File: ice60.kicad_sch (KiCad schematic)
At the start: 31 parts, among them J1 SWD, J2 JST SH 4-pin, SW1 SW_Push, U1 RP2040, U2 W25Q128JVS, U3 XC6206PxxxMR-Regulator_Linear, U4 SRV05-4, Y1 12MHz

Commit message: rearrange schematic
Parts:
- renumbered C4 to C2, C5 to C3, C2 to C4, C3 to C5
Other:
- moved on the sheet: C1, C10, C11, C12, C13, C14, C15, C16, C17, C2, C3, C4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

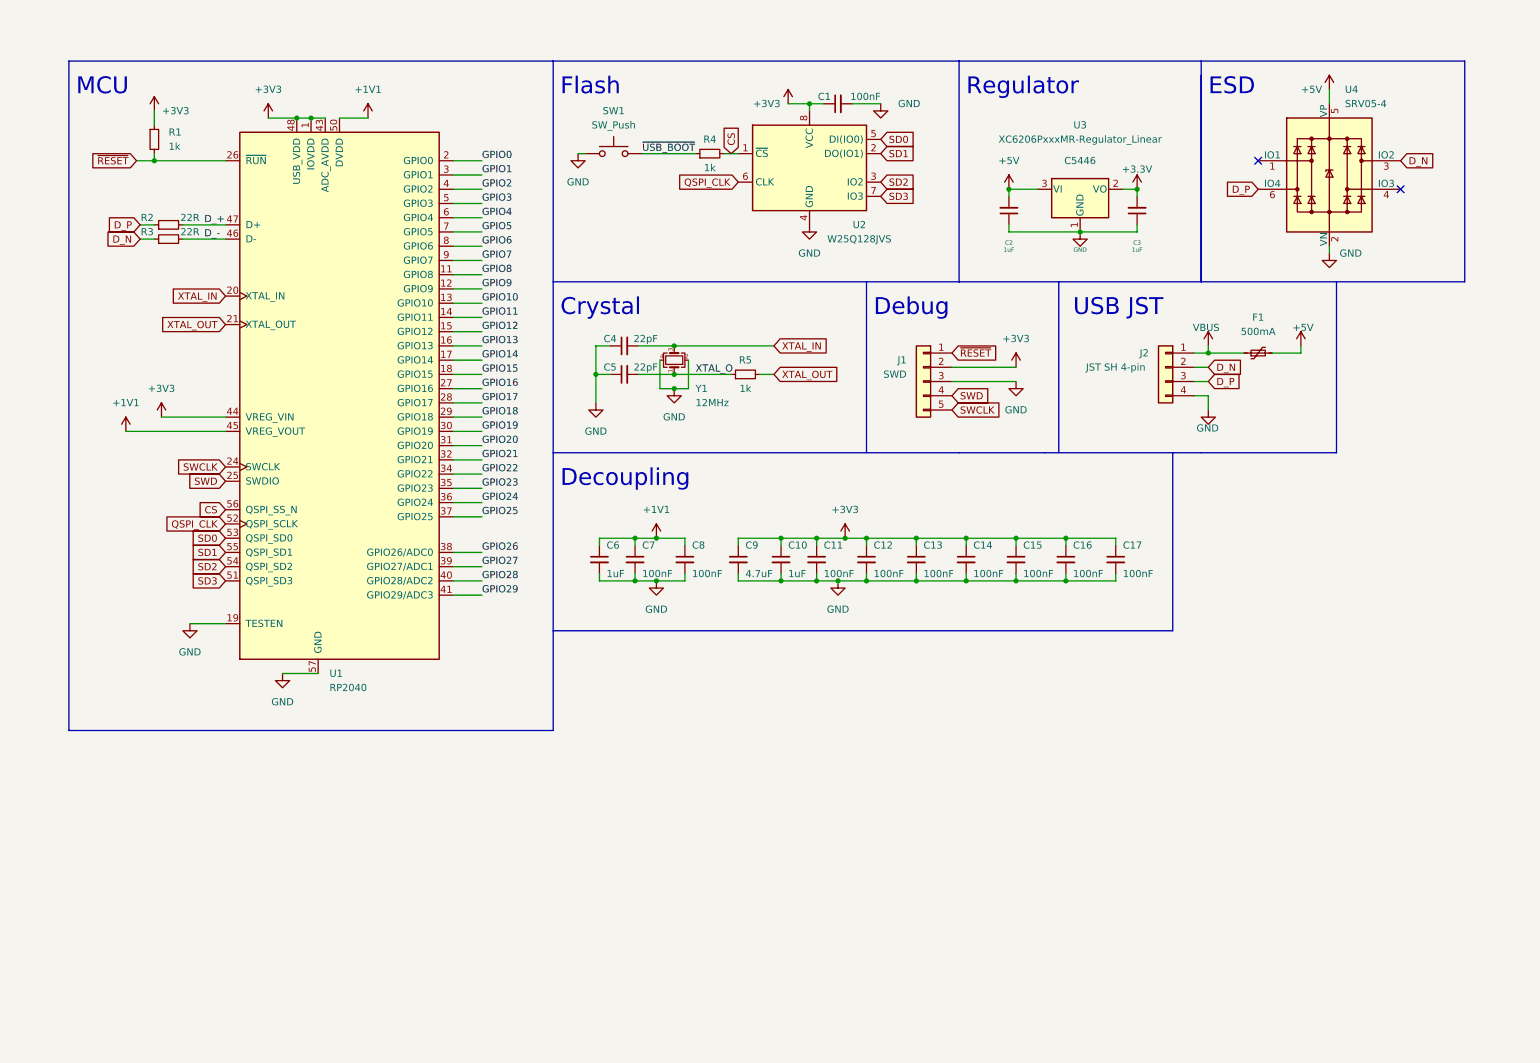
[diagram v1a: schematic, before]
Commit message: initial matrix schematic
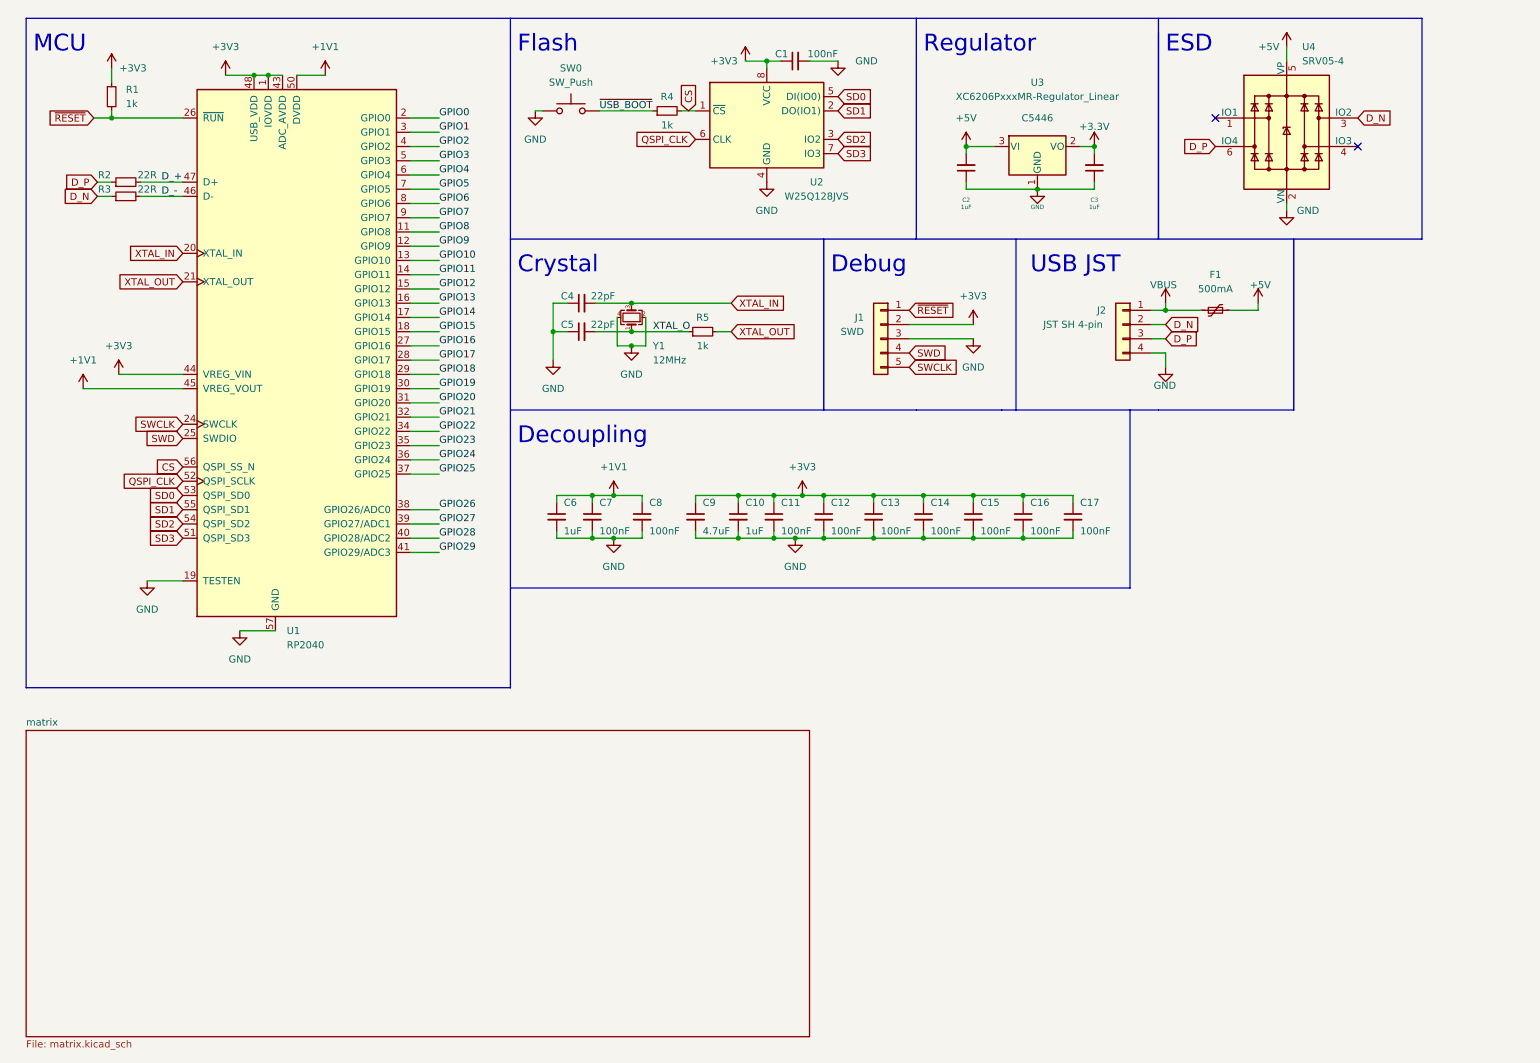
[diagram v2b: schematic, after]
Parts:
- renumbered SW1 to SW0
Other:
- added sheet matrix (matrix.kicad_sch)
- moved on the sheet: C1, C10, C11, C12, C13, C14, C15, C16, C17, C2, C3, C4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

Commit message: clean up
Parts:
- removed J2: JST SH 4-pin, Connector_JST:JST_SH_SM04B-SRSS-TB_1x04-1MP_P1.00mm_Horizontal, symbol bakeneko-60-pcb-rescue:Conn_01x04-Connector_Generic
- removed U1: RP2040, Sleep-Lib:RP2040-QFN-56, symbol Sleep-lib:RP2040
- removed U3: XC6206PxxxMR-Regulator_Linear, Package_TO_SOT_SMD:SOT-23, symbol kicad-keyboard-parts:XC6206PxxxMR-Regulator_Linear
- added J2: JST SH 4-pin, Connector_JST:JST_SH_SM04B-SRSS-TB_1x04-1MP_P1.00mm_Horizontal, symbol Connector_Generic:Conn_01x04
- added U1: RP2040, Sleep-Lib:RP2040-QFN-56, symbol Sleep-Lib:RP2040
- added U3: XC6206PxxxMR, Package_TO_SOT_SMD:SOT-23, symbol Regulator_Linear:XC6206PxxxMR
- F1: LCSC C70076 -> (none)
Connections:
- net +1V1: now also U1.23 (DVDD), U1.45 (VREG_VOUT), U1.50 (DVDD)
- net +3V3: now also U1.1 (IOVDD), U1.10 (IOVDD), U1.22 (IOVDD), U1.33 (IOVDD), U1.42 (IOVDD), U1.43 (ADC_AVDD), U1.44 (VREG_VIN), U1.48 (USB_VDD), U1.49 (IOVDD), U3.2 (VO)
- net +5V: now also U3.3 (VI)
- net CS: now also U1.56 (QSPI_SS_N)
- net D_+: now also U1.47 (D+)
- net D_-: now also U1.46 (D-)
- net D_N: now also J2.2 (Pin_2)
- net D_P: now also J2.3 (Pin_3)
- net GND: now also J2.4 (Pin_4), U1.19 (TESTEN), U1.57 (GND), U3.1 (GND)
- net QSPI_CLK: now also U1.52 (QSPI_SCLK)
- net SD0: now also U1.53 (QSPI_SD0)
- net SD1: now also U1.55 (QSPI_SD1)
- net SD2: now also U1.54 (QSPI_SD2)
- net SD3: now also U1.51 (QSPI_SD3)
- net SWCLK: now also U1.24 (SWCLK)
- net SWD: now also U1.25 (SWDIO)
- net VBUS: now also J2.1 (Pin_1)
- net XTAL_IN: now also U1.20 (XTAL_IN)
- net XTAL_OUT: now also U1.21 (XTAL_OUT)
- net ~{RESET}: now also U1.26 (~{RUN})
- no-connect marks 2 -> 32

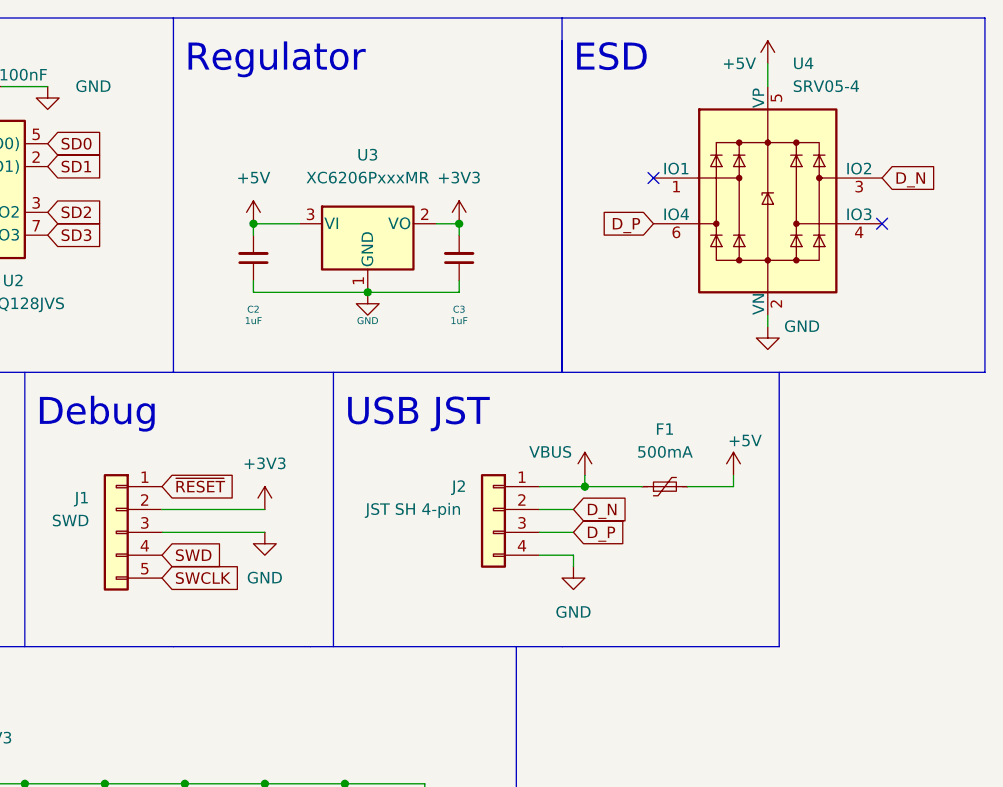
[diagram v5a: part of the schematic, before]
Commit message: preliminary SMD component placements
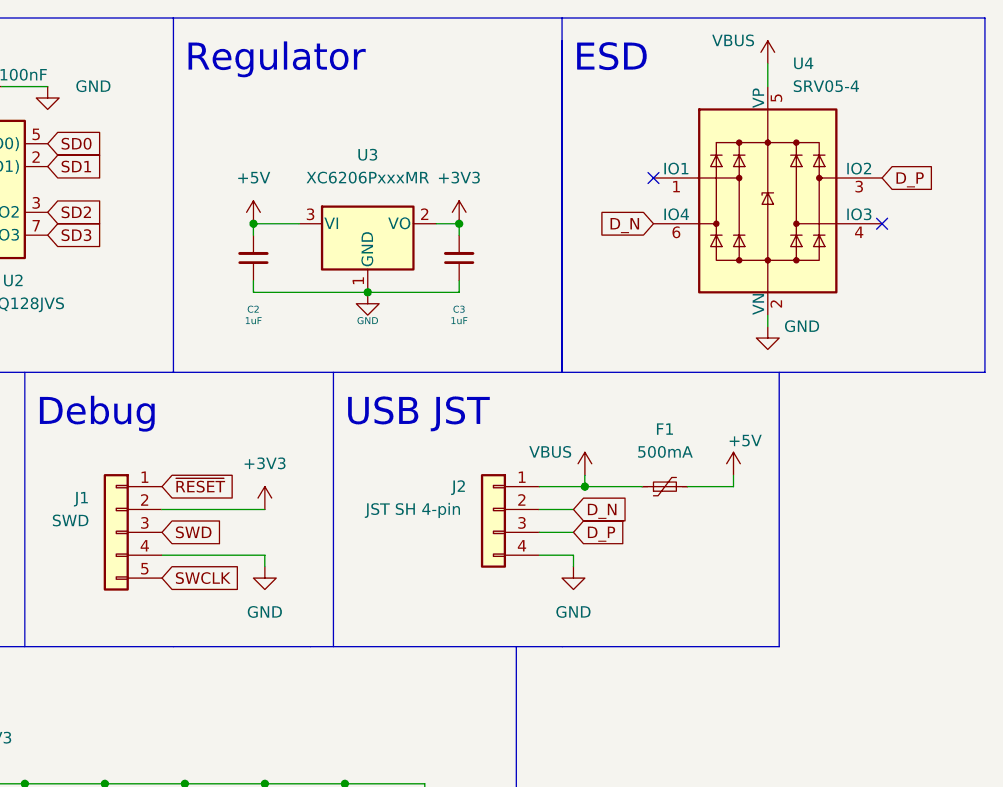
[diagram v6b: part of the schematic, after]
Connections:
- net +5V: no longer U4.5 (VP)
- net D_N: now also U4.6 (IO4); no longer U4.3 (IO2)
- net D_P: now also U4.3 (IO2); no longer U4.6 (IO4)
- net GND: now also J1.4 (Pin_4); no longer J1.3 (Pin_3)
- net SWD: now also J1.3 (Pin_3); no longer J1.4 (Pin_4)
- net VBUS: now also U4.5 (VP)
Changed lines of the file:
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@@
     (stroke (width 0) (type solid) (color 0 0 0 0))
-  )
-  (wire (pts (xy 184.15 72.39) (xy 172.72 72.39))
-    (stroke (width 0) (type default) (color 0 0 0 0))
   )
   (wire (pts (xy 125.095 107.95) (xy 125.095 106.68))
@@
     (stroke (width 0) (type default) (color 0 0 0 0))
   )
+  (wire (pts (xy 172.72 74.93) (xy 184.15 74.93))
+    (stroke (width 0) (type default) (color 0 0 0 0))
+  )
   (wire (pts (xy 148.59 100.33) (xy 153.67 100.33))
     (stroke (width 0) (type default) (color 0 0 0 0))
@@
   )
   (wire (pts (xy 166.37 100.33) (xy 175.26 100.33))
+    (stroke (width 0) (type default) (color 0 0 0 0))
+  )
+  (wire (pts (xy 184.15 76.2) (xy 184.15 74.93))
     (stroke (width 0) (type default) (color 0 0 0 0))
   )
@@
     )
   )
-  (global_label "SWD" (shape input) (at 172.72 74.93 0) (fields_autoplaced)
-    (effects (font (size 1.27 1.27)) (justify left))
-    (property "Intersheet References" "${INTERSHEET_REFS}" (id 0) (at 179.0641 74.8506 0)
-      (effects (font (size 1.27 1.27)) (justify left) hide)
-    )
-  )
   (global_label "XTAL_OUT" (shape input) (at 43.18 62.23 180) (fields_autoplaced)
     (effects (font (size 1.27 1.27)) (justify right))
@@
     )
   )
-  (global_label "D_N" (shape input) (at 252.73 33.02 0) (fields_autoplaced)
+  (global_label "D_P" (shape input) (at 252.73 33.02 0) (fields_autoplaced)
     (effects (font (size 1.27 1.27)) (justify left))
-    (property "Intersheet References" "${INTERSHEET_REFS}" (id 0) (at 258.7112 32.9406 0)
+    (property "Intersheet References" "${INTERSHEET_REFS}" (id 0) (at 258.6507 32.9406 0)
       (effects (font (size 1.27 1.27)) (justify left) hide)
     )
@@
     )
   )
-  (global_label "D_P" (shape input) (at 227.33 38.1 180) (fields_autoplaced)
+  (global_label "D_N" (shape input) (at 227.33 38.1 180) (fields_autoplaced)
     (effects (font (size 1.27 1.27)) (justify right))
-    (property "Intersheet References" "${INTERSHEET_REFS}" (id 0) (at 221.4093 38.0206 0)
+    (property "Intersheet References" "${INTERSHEET_REFS}" (id 0) (at 221.3488 38.0206 0)
       (effects (font (size 1.27 1.27)) (justify right) hide)
     )
@@
     )
   )
+  (global_label "SWD" (shape input) (at 172.72 72.39 0) (fields_autoplaced)
+    (effects (font (size 1.27 1.27)) (justify left))
+    (property "Intersheet References" "${INTERSHEET_REFS}" (id 0) (at 179.0641 72.3106 0)
+      (effects (font (size 1.27 1.27)) (justify left) hide)
+    )
+  )
   (symbol (lib_id "Device:C_Small") (at 175.26 104.14 0) (unit 1)
     (in_bom yes) (on_board yes)
@@
     (pin "1")
     (pin "2")
-  )
-  (symbol (lib_id "power:+5V") (at 240.03 20.32 0) (mirror y) (unit 1)
-    (in_bom yes) (on_board yes)
-    (property "Reference" "#PWR017" (id 0) (at 240.03 24.13 0)
-      (effects (font (size 1.27 1.27)) hide)
-    )
-    (property "Value" "+5V" (id 1) (at 236.855 20.32 0))
-    (property "Footprint" "" (id 2) (at 240.03 20.32 0)
-      (effects (font (size 1.27 1.27)) hide)
-    )
-    (property "Datasheet" "" (id 3) (at 240.03 20.32 0)
-      (effects (font (size 1.27 1.27)) hide)
-    )
-    (pin "1")
   )
   (symbol (lib_id "power:GND") (at 218.44 76.2 0) (unit 1)
@@
     (pin "1")
   )
+  (symbol (lib_id "power:VBUS") (at 240.03 20.32 0) (unit 1)
+    (in_bom yes) (on_board yes)
+    (property "Reference" "#PWR0104" (id 0) (at 240.03 24.13 0)
+      (effects (font (size 1.27 1.27)) hide)
+    )
+    (property "Value" "VBUS" (id 1) (at 236.22 17.78 0))
+    (property "Footprint" "" (id 2) (at 240.03 20.32 0)
+      (effects (font (size 1.27 1.27)) hide)
+    )
+    (property "Datasheet" "" (id 3) (at 240.03 20.32 0)
+      (effects (font (size 1.27 1.27)) hide)
+    )
+    (pin "1")
+  )
   (symbol (lib_id "Device:C_Small") (at 201.93 104.14 0) (unit 1)
     (in_bom yes) (on_board yes)
@@
     (pin "1")
   )
-  (symbol (lib_id "power:GND") (at 184.15 72.39 0) (unit 1)
-    (in_bom yes) (on_board yes) (fields_autoplaced)
-    (property "Reference" "#PWR022" (id 0) (at 184.15 78.74 0)
-      (effects (font (size 1.27 1.27)) hide)
-    )
-    (property "Value" "GND" (id 1) (at 184.15 77.47 0))
-    (property "Footprint" "" (id 2) (at 184.15 72.39 0)
-      (effects (font (size 1.27 1.27)) hide)
-    )
-    (property "Datasheet" "" (id 3) (at 184.15 72.39 0)
+  (symbol (lib_id "power:GND") (at 184.15 76.2 0) (unit 1)
+    (in_bom yes) (on_board yes) (fields_autoplaced)
+    (property "Reference" "#PWR022" (id 0) (at 184.15 82.55 0)
+      (effects (font (size 1.27 1.27)) hide)
+    )
+    (property "Value" "GND" (id 1) (at 184.15 81.28 0))
+    (property "Footprint" "" (id 2) (at 184.15 76.2 0)
+      (effects (font (size 1.27 1.27)) hide)
+    )
+    (property "Datasheet" "" (id 3) (at 184.15 76.2 0)
       (effects (font (size 1.27 1.27)) hide)
     )
@@
       (reference "#PWR016") (unit 1) (value "GND") (footprint "")
     )
-    (path "/08b49b14-3af1-4660-9ce3-de3c0508b207"
-      (reference "#PWR017") (unit 1) (value "+5V") (footprint "")
-    )
     (path "/f3b88008-55a9-4f90-959e-db99547a1a4d"
       (reference "#PWR018") (unit 1) (value "GND") (footprint "")
@@
       (reference "#PWR0103") (unit 1) (value "+5V") (footprint "")
     )
+    (path "/c0c66f86-c595-4f2a-9602-6a596e4bd319"
+      (reference "#PWR0104") (unit 1) (value "VBUS") (footprint "")
+    )
     (path "/56077389-3dc3-4dac-9d26-70524308becc"

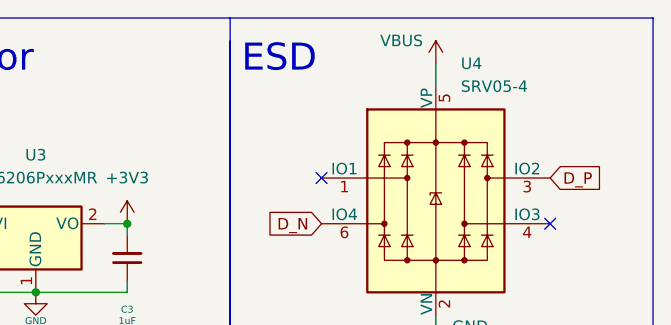
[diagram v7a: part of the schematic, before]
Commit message: wire up most things other than matrix
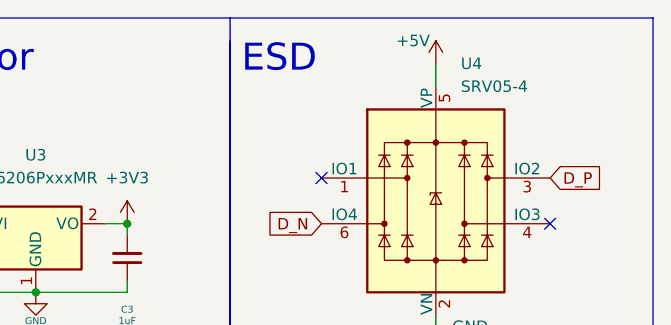
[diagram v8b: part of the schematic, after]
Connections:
- net +5V: now also U4.5 (VP)
- net VBUS: no longer U4.5 (VP)
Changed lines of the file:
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@@
     (pin "2")
+  )
+  (symbol (lib_id "power:+5V") (at 240.03 20.32 0) (unit 1)
+    (in_bom yes) (on_board yes)
+    (property "Reference" "#PWR?" (id 0) (at 240.03 24.13 0)
+      (effects (font (size 1.27 1.27)) hide)
+    )
+    (property "Value" "+5V" (id 1) (at 237.49 17.78 0))
+    (property "Footprint" "" (id 2) (at 240.03 20.32 0)
+      (effects (font (size 1.27 1.27)) hide)
+    )
+    (property "Datasheet" "" (id 3) (at 240.03 20.32 0)
+      (effects (font (size 1.27 1.27)) hide)
+    )
+    (pin "1")
   )
   (symbol (lib_id "Switch:SW_Push") (at 112.395 31.75 0) (unit 1)
@@
     )
     (property "Datasheet" "" (id 3) (at 182.88 38.1 0)
-      (effects (font (size 1.27 1.27)) hide)
-    )
-    (pin "1")
-  )
-  (symbol (lib_id "power:VBUS") (at 240.03 20.32 0) (unit 1)
-    (in_bom yes) (on_board yes)
-    (property "Reference" "#PWR0104" (id 0) (at 240.03 24.13 0)
-      (effects (font (size 1.27 1.27)) hide)
-    )
-    (property "Value" "VBUS" (id 1) (at 236.22 17.78 0))
-    (property "Footprint" "" (id 2) (at 240.03 20.32 0)
-      (effects (font (size 1.27 1.27)) hide)
-    )
-    (property "Datasheet" "" (id 3) (at 240.03 20.32 0)
       (effects (font (size 1.27 1.27)) hide)
     )
@@
       (reference "#PWR0103") (unit 1) (value "+5V") (footprint "")
     )
-    (path "/c0c66f86-c595-4f2a-9602-6a596e4bd319"
-      (reference "#PWR0104") (unit 1) (value "VBUS") (footprint "")
+    (path "/98dd4e45-1185-44d2-8220-7a892da24295"
+      (reference "#PWR?") (unit 1) (value "+5V") (footprint "")
     )
     (path "/56077389-3dc3-4dac-9d26-70524308becc"
